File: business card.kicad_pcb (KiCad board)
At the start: 2 copper layers, 89.4 x 51 mm, 4 parts, among them U1 NT3H1101_NT3H1201

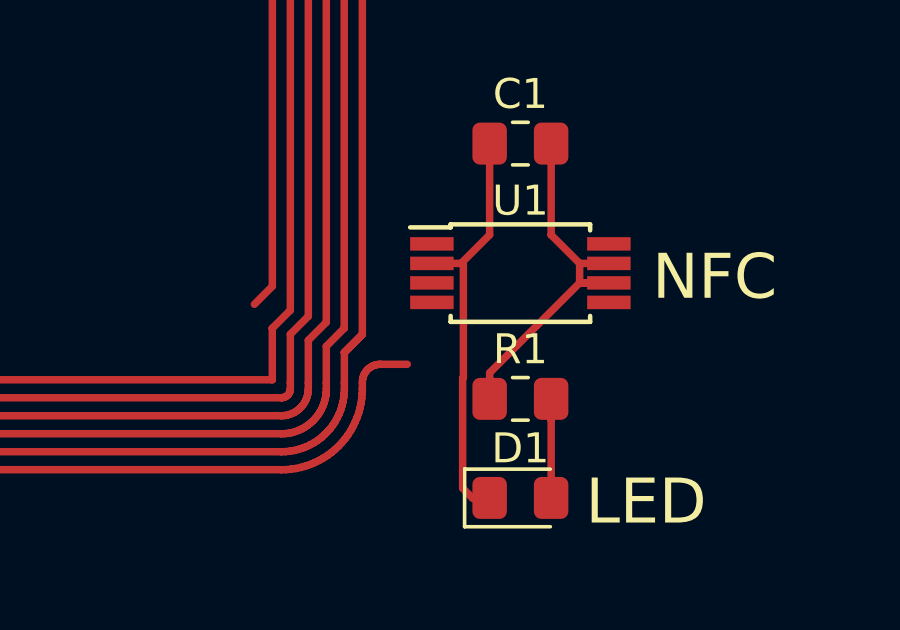
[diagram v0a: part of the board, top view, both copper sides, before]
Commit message: Added all traces
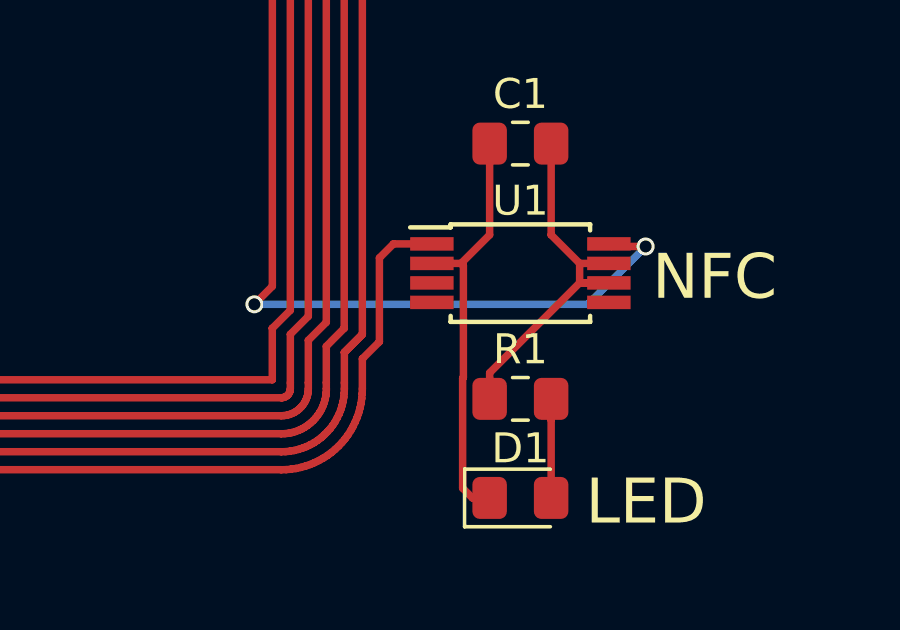
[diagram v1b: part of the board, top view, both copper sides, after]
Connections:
- U1 pad 1: Net-(L1-Pad1) -> Net-(U1-Pad1)
- U1 pad 8: Net-(L1-Pad2) -> Net-(U1-Pad1)
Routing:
- net Net-(U1-Pad1): track 0.00 -> 721.1 mm, vias 0 -> 2
- net (no net): track 701.5 -> 0.00 mm
